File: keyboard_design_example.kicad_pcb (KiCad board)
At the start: 2 copper layers, 34 parts, among them SW1 SW_PUSH, U1 ATmega32U4-AU, Y1 16MHz

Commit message: Update
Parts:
- moved R1 9.53 mm to (87.3, 91.3)
- moved USB1 9.53 mm to (77.8, 89.7)
- moved R2 9.52 mm to (87.3, 88.9)
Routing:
- net GND: track 107.0 -> 117.1 mm
- net Net-(R2-Pad1): track 40.4 -> 50.4 mm
- net ROW2: track 113.1 -> 103.5 mm
- net Net-(R1-Pad1): track 38.7 -> 48.3 mm
- net VCC: track 7.87 -> 17.4 mm
- net ROW0: track 100.1 -> 98.6 mm

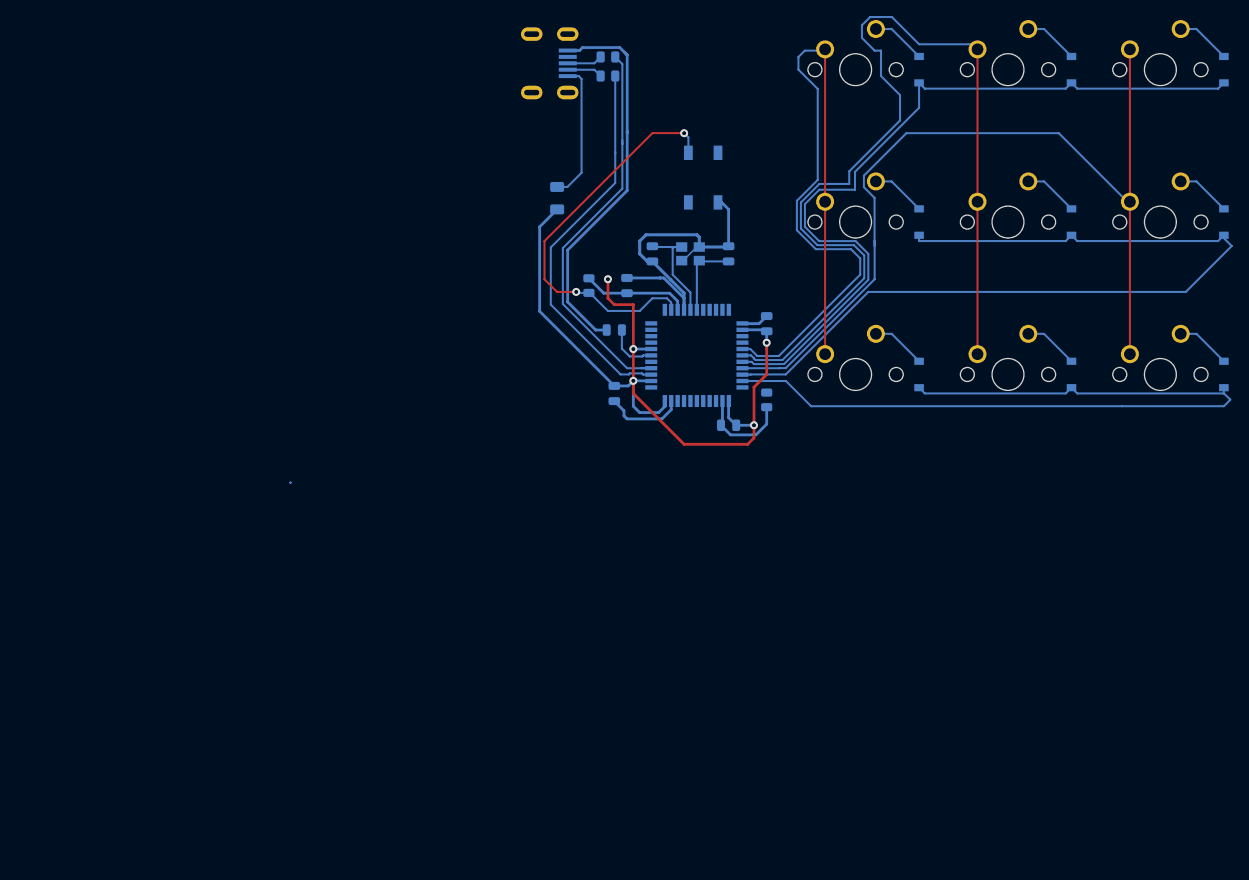
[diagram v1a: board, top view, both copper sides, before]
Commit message: Vertical MCU/usb
Made the usb and MCU face vertically and rewired the switch matrix to the mcu
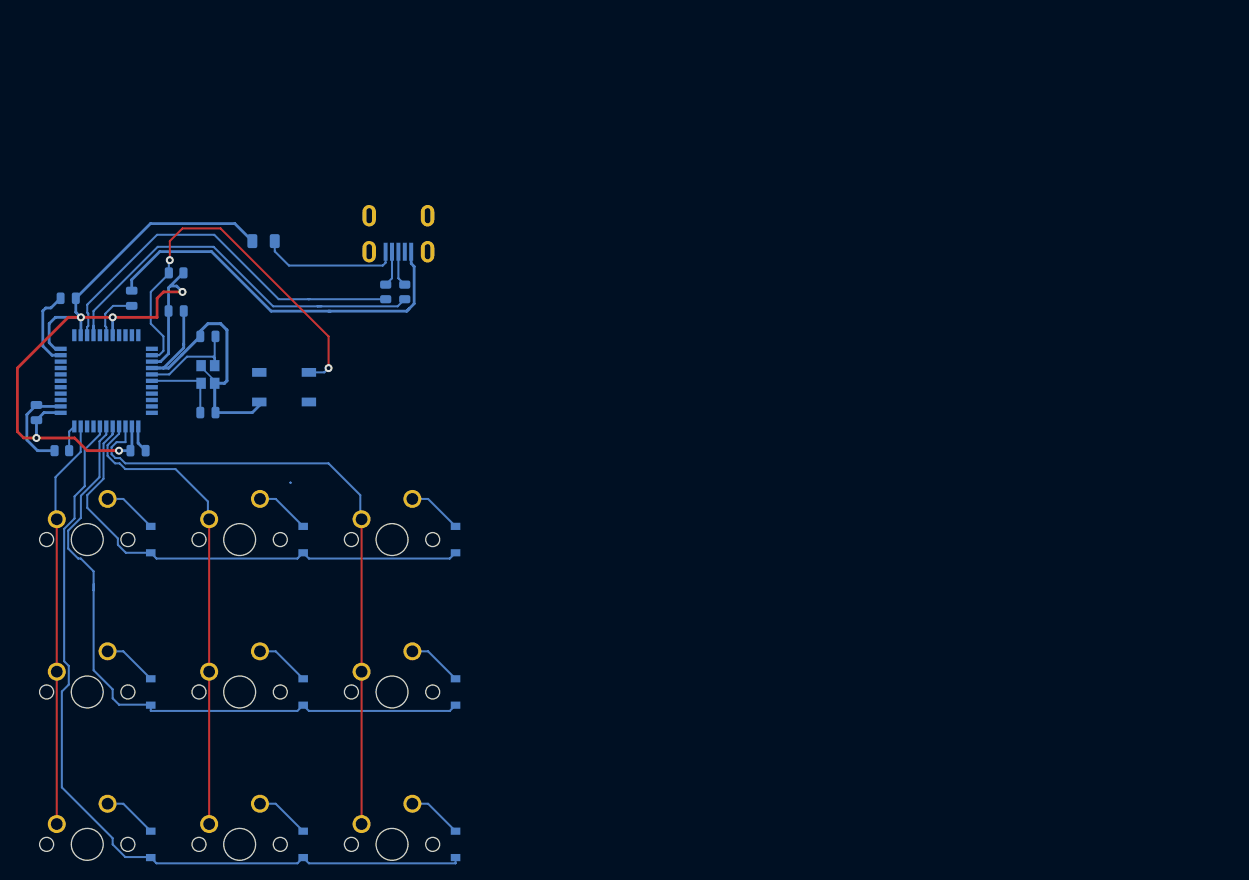
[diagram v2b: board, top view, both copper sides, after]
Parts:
- moved D3 112.6 mm to (68.3, 149.2)
- moved D6 112.6 mm to (68.3, 168.3)
- moved MX3 112.6 mm to (60.3, 149.2)
- moved MX6 112.6 mm to (60.3, 168.3)
- moved D1 112.6 mm to (30.2, 149.2)
- moved D2 112.6 mm to (49.2, 149.2)
- moved D4 112.6 mm to (30.2, 168.3)
- moved D5 112.6 mm to (49.2, 168.3)
- moved D9 112.6 mm to (68.3, 187.3)
- moved MX1 112.6 mm to (22.2, 149.2)
- moved MX2 112.6 mm to (41.3, 149.2)
- moved MX4 112.6 mm to (22.2, 168.3)
- moved MX5 112.6 mm to (41.3, 168.3)
- moved MX9 112.6 mm to (60.3, 187.3)
- moved D7 112.6 mm to (30.2, 187.3)
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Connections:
- U1 pad 25: Net-(U1-Pad25) -> COL2
- U1 pad 26: Net-(U1-Pad26) -> COL1
- U1 pad 27: COL0 -> ROW0
- U1 pad 28: COL1 -> ROW1
- U1 pad 29: ROW0 -> ROW2
- U1 pad 30: COL2 -> Net-(U1-Pad30)
- U1 pad 31: ROW1 -> Net-(U1-Pad31)
- U1 pad 32: ROW2 -> COL0
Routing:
- net COL1: track 121.7 -> 60.5 mm
- net COL0: track 96.3 -> 51.3 mm
- net ROW0: track 98.6 -> 61.6 mm
- net COL2: track 112.3 -> 79.6 mm
- net ROW1: track 109.3 -> 84.1 mm
- net Net-(R4-Pad2): track 0.00 -> 3.30 mm
- net +5V: track 113.6 -> 115.4 mm
- net ROW2: track 103.5 -> 102.5 mm
